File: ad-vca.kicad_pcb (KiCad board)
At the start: 2 copper layers, 96.6 x 128.5 mm, 74 parts, among them J1 Eurorack_Power_10pin_Unshroud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, J10 Conn_01x04, J11 Conn_01x04, J12 Conn_01x04, J13 Conn_01x04, J14 Conn_01x04, J15 Conn_01x04, J2 Conn_01x04, J3 PJ301M-12, J4 PJ301M-12, J5 PJ301M-12, J6 PJ301M-12, J7 Conn_01x04, J8 Conn_01x04, J9 Conn_01x04, Q1 2N3904, Q2 2N3904, Q3 2N3904, Q4 2N3904, Q5 2N3904, SW1 SW_SPDT, U1 TL074, U2 TL074

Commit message: First print round
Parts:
- added C4: 1uF_0603_25V, Capacitor_THT:C_Disc_D3.8mm_W2.6mm_P2.50mm, F.Cu at (98.3, 143.0)
- added C5: 1uF_0603_25V, Capacitor_THT:C_Disc_D3.8mm_W2.6mm_P2.50mm, F.Cu at (96.0, 139.3)
- added C6: 10uf, Capacitor_THT:CP_Radial_D4.0mm_P2.00mm, B.Cu at (104.0, 133.0)
- added C7: 10uf, Capacitor_THT:CP_Radial_D4.0mm_P2.00mm, B.Cu at (104.0, 125.1)
- C1: footprint Capacitor_THT:C_Axial_L3.8mm_D2.6mm_P7.50mm_Horizontal -> Capacitor_THT:C_Disc_D3.0mm_W1.6mm_P2.50mm
- C2: footprint Capacitor_THT:C_Disc_D3.8mm_W2.6mm_P2.50mm -> Capacitor_THT:C_Disc_D3.0mm_W1.6mm_P2.50mm
- J12, J13, J14, J8, J9: moved to B.Cu
- moved R14 7.51 mm to (115.5, 101.8)
- moved J11 7.30 mm to (115.6, 105.2)
- moved R10 6.51 mm to (115.5, 128.5)
- moved D2 6.51 mm to (113.0, 67.2)
- moved Q2 6.51 mm to (98.8, 90.4)
- moved R1 6.51 mm to (99.6, 67.7)
- moved R11 6.51 mm to (108.8, 108.4)
- moved R17 6.51 mm to (102.8, 101.5)
- moved R19 6.51 mm to (102.9, 116.6)
- moved R23 6.51 mm to (115.7, 84.2)
- moved R35 6.51 mm to (102.6, 84.5)
- moved C1 6.51 mm to (115.8, 49.6)
- moved D5 6.51 mm to (99.4, 38.8)
- moved J10 6.51 mm to (96.3, 39.0)
- moved J7 6.51 mm to (115.6, 39.0)
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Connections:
- J3 pad 3: unconnected-(J3-Pad3) -> /Control Panel/GND
- J4 pad 3: unconnected-(J4-Pad3) -> /Control Panel/GND
- J5 pad 3: unconnected-(J5-Pad3) -> /Control Panel/GND
- J6 pad 3: unconnected-(J6-Pad3) -> /Control Panel/GND
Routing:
- net /Control Panel/GND: track 61.2 -> 118.4 mm
- net GND: track 212.2 -> 236.5 mm, vias 9 -> 8
- net -12V: track 119.1 -> 138.1 mm
- net +12V: track 142.5 -> 160.4 mm
- net Net-(D1-A): track 22.7 -> 26.9 mm
- net Net-(R23-Pad2): track 82.6 -> 80.3 mm
- net Net-(D3-A): track 30.1 -> 32.2 mm
- net Net-(R33-Pad2): track 60.7 -> 62.7 mm
- net Net-(Q1-E): track 31.6 -> 29.7 mm
- net /Control Panel/Attack 1: track 80.7 -> 79.0 mm
- net /Circuit Panel/lfo pot 1: track 34.8 -> 36.4 mm
- net /Circuit Panel/lfo pot 2: track 28.5 -> 30.0 mm
- net Net-(Q5-C): track 36.9 -> 35.8 mm
- net Net-(Q2-C): track 62.6 -> 63.6 mm
- net /Control Panel/lfo rate 2: track 26.9 -> 26.3 mm
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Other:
- board size 96.6 x 128.5 mm -> 102.4 x 128.5 mm

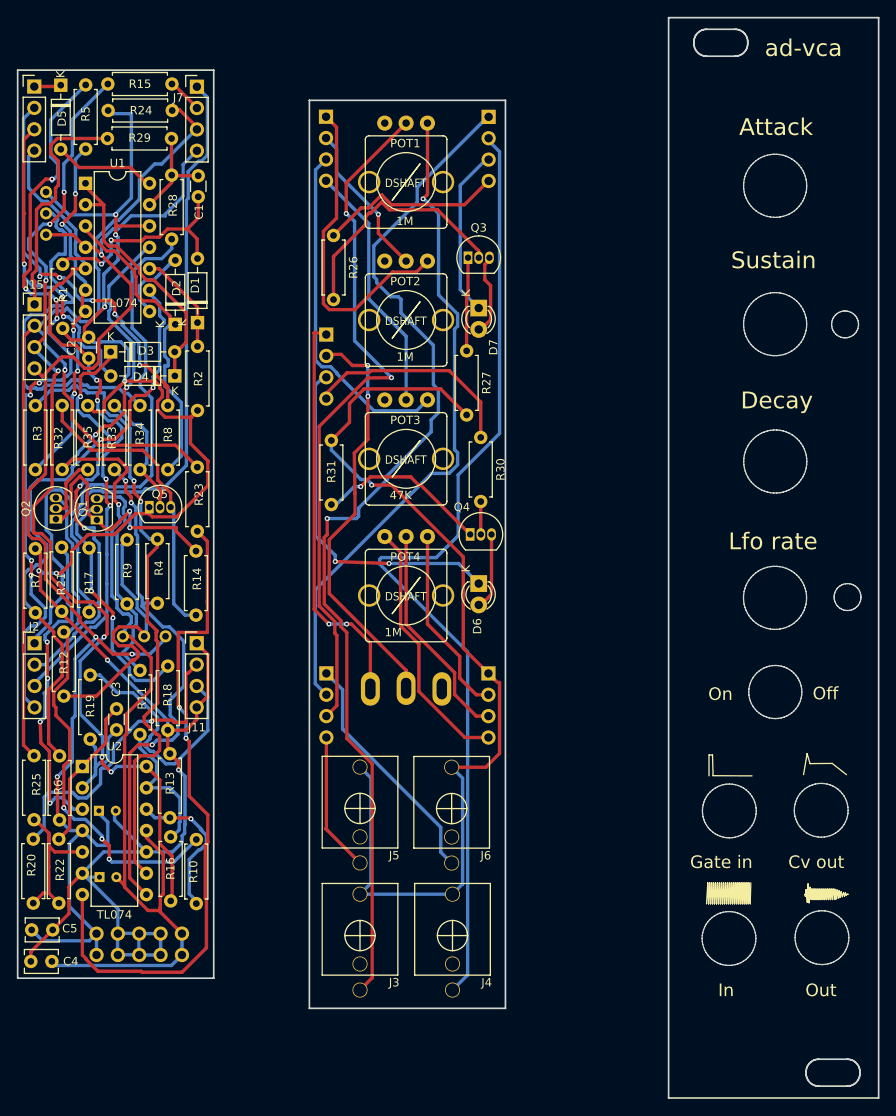
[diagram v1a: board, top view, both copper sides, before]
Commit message: Fixed bad tracing and reviewed circuit design
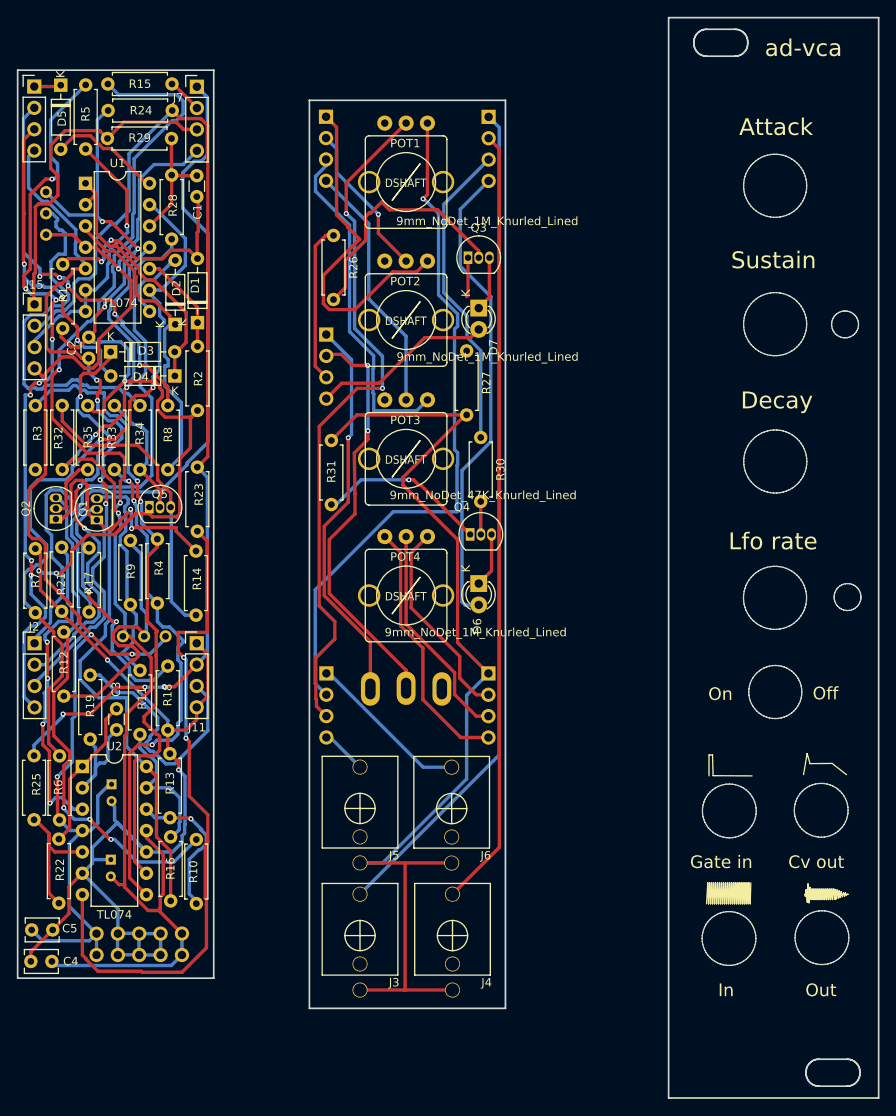
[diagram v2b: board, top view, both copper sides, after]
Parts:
- removed R20: 100k_0603, Resistor_THT:R_Axial_DIN0207_L6.3mm_D2.5mm_P7.62mm_Horizontal
- POT1, POT2, POT4: value 1M -> 9mm_NoDet_1M_Knurled_Lined
- POT3: value 47K -> 9mm_NoDet_47K_Knurled_Lined
- moved C7 3.49 mm to (105.5, 121.9), turned to -90 degrees
- moved C6 2.48 mm to (105.4, 130.9), turned to -90 degrees
- moved R9 0.41 mm to (107.7, 92.9)
- moved C1 0.17 mm to (115.6, 49.5)
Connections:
- C1 pad 1: Net-(U1D--) -> Net-(U1D-+)
- D6 pad 1: /Control Panel/led 2 - -> Net-(D6-K)
- D6 pad 2: Net-(D6-A) -> /Control Panel/led 1 +
- D7 pad 1: /Control Panel/led 1 - -> Net-(D7-K)
- D7 pad 2: Net-(D7-A) -> /Control Panel/led 2 +
- J15 pad 1: /Circuit Panel/lfo switch 1 -> /Circuit Panel/lfo led 1 -
- J15 pad 2: /Circuit Panel/lfo led 1 - -> /Circuit Panel/lfo pot 1
- J3 pad 1: /Control Panel/Audio In -> /Control Panel/GND
- J3 pad 3: /Control Panel/GND -> /Control Panel/Audio In
- J4 pad 1: /Control Panel/Audio Out -> /Control Panel/GND
- J4 pad 3: /Control Panel/GND -> /Control Panel/Audio Out
- J5 pad 1: /Control Panel/Cv out -> /Control Panel/GND
- J5 pad 3: /Control Panel/GND -> /Control Panel/Cv out
- J6 pad 1: /Control Panel/Gate In -> /Control Panel/GND
- J6 pad 3: /Control Panel/GND -> /Control Panel/Gate In
- Q3 pad 3: Net-(D7-A) -> Net-(D7-K)
- Q4 pad 3: Net-(D6-A) -> Net-(D6-K)
- R15 pad 1: /Circuit Panel/adsr led 2 - -> Net-(R15-Pad1)
- R16 pad 2: /Circuit Panel/adsr led 2 - -> Net-(R15-Pad1)
- R23 pad 1: /Circuit Panel/lfo led 1 - -> /Circuit Panel/lfo pot 1
- R24 pad 1: /Circuit Panel/lfo led 1 - -> /Circuit Panel/lfo pot 1
- R25 pad 1: /Circuit Panel/lfo led 1 - -> /Circuit Panel/lfo pot 1
- R26 pad 1: /Control Panel/led 1 + -> /Control Panel/led 2 -
- R28 pad 1: Net-(U1D--) -> Net-(U1D-+)
- R29 pad 1: Net-(U1D--) -> Net-(U1D-+)
- R29 pad 2: /Circuit Panel/lfo switch 1 -> /Circuit Panel/lfo led 1 -
- R3 pad 1: Net-(U1B--) -> /Circuit Panel/adsr led 2 -
- R30 pad 1: /Control Panel/led 2 + -> /Control Panel/led 1 -
- R5 pad 2: Net-(U1B--) -> /Circuit Panel/adsr led 2 -
- U1 pad 12: GND -> Net-(U1D-+)
- U1 pad 13: Net-(U1D--) -> Net-(U1C--)
- U1 pad 6: Net-(U1B--) -> /Circuit Panel/adsr led 2 -
- U1 pad 7: Net-(U1B--) -> /Circuit Panel/adsr led 2 -
- U2 pad 14: /Circuit Panel/adsr led 2 - -> Net-(R15-Pad1)
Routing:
- net Net-(R15-Pad1): track 0.00 -> 126.9 mm, vias 0 -> 2
- net /Circuit Panel/lfo pot 1: track 36.4 -> 130.0 mm, vias 1 -> 3
- net /Circuit Panel/adsr led 2 -: track 120.8 -> 32.5 mm, vias 7 -> 1
- net /Circuit Panel/lfo led 1 -: track 123.9 -> 40.9 mm, vias 1 -> 0
- net Net-(U1B--): track 44.2 -> 0.00 mm, vias 5 -> 0
- net /Control Panel/led 1 +: track 21.9 -> 56.5 mm
- net /Circuit Panel/lfo switch 1: track 28.5 -> 0.00 mm
- net /Control Panel/Audio In: track 123.7 -> 99.8 mm, vias 1 -> 0
- net /Control Panel/Audio Out: track 116.6 -> 92.7 mm
- net /Control Panel/led 2 -: track 41.7 -> 18.8 mm, vias 2 -> 0
- net /Control Panel/led 1 -: track 20.2 -> 37.1 mm
- net Net-(U1D-+): track 0.00 -> 15.2 mm
- net Net-(U1C--): track 71.5 -> 86.2 mm
- net Net-(U1D--): track 12.7 -> 0.00 mm
- net /Control Panel/Cv out: track 16.8 -> 5.46 mm
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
